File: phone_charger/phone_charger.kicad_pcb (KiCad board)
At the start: 2 copper layers, 22.6 x 30.8 mm, 19 parts, among them J1 Conn_01x02, J2 UE27AC54100, U1 ADP2302

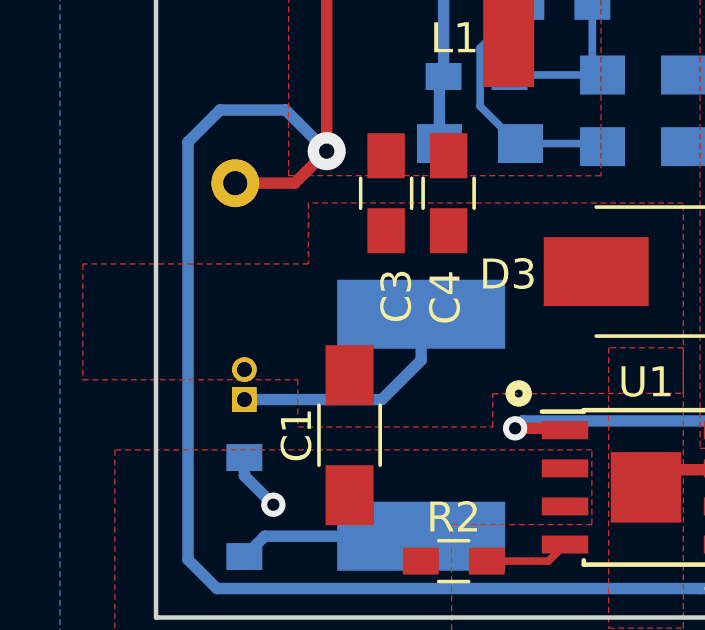
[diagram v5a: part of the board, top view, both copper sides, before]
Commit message: Updated header footprint for charger layout
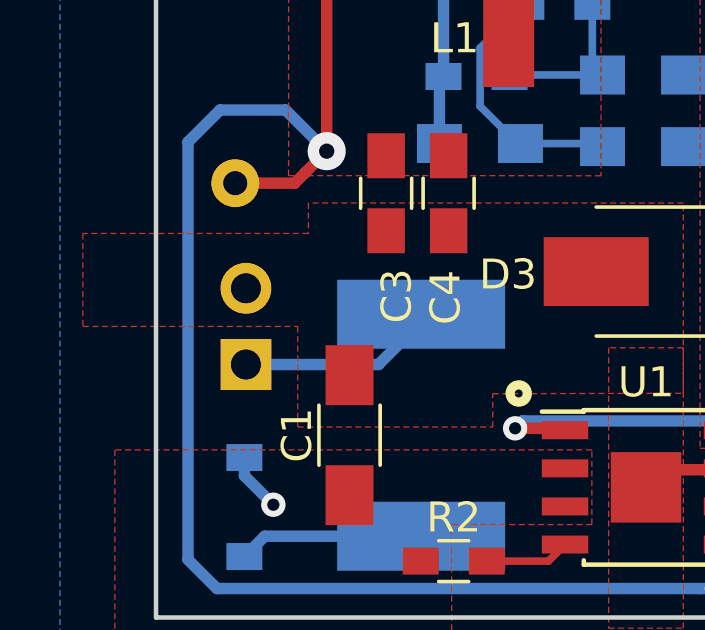
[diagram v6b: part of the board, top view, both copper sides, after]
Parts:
- J1: footprint Pin_Headers:Pin_Header_Straight_1x02_Pitch1.00mm -> Pin_Headers:Pin_Header_Straight_1x02_Pitch2.54mm
- moved J1 1.17 mm to (90.5, 76.0)
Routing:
- net Net-(F1-Pad2): track 7.97 -> 6.69 mm
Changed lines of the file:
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@@
     (add_net VBUS)
+  )
+  (module Pin_Headers:Pin_Header_Straight_1x02_Pitch2.54mm (layer B.Cu)
+    (at 90.5256 75.9968)
+    (descr "Through hole straight pin header, 1x02, 2.54mm pitch, single row")
+    (tags "Through hole pin header THT 1x02 2.54mm single row")
+    (fp_text reference J1 (at 0 2.33) (layer B.SilkS)
+      (effects (font (size 1 1) (thickness 0.15)) (justify mirror))
+    )
+    (fp_text value Conn_01x02 (at 0 -4.87) (layer B.Fab)
+      (effects (font (size 1 1) (thickness 0.15)) (justify mirror))
+    )
+    (fp_text user %R (at 0 -1.27 -90) (layer B.Fab)
+      (effects (font (size 1 1) (thickness 0.15)) (justify mirror))
+    )
+    (fp_line (start 1.8 1.8) (end -1.8 1.8) (layer B.CrtYd) (width 0.05))
+    (fp_line (start 1.8 -4.35) (end 1.8 1.8) (layer B.CrtYd) (width 0.05))
+    (fp_line (start -1.8 -4.35) (end 1.8 -4.35) (layer B.CrtYd) (width 0.05))
+    (fp_line (start -1.8 1.8) (end -1.8 -4.35) (layer B.CrtYd) (width 0.05))
+    (fp_line (start -1.33 1.33) (end 0 1.33) (layer B.SilkS) (width 0.12))
+    (fp_line (start -1.33 0) (end -1.33 1.33) (layer B.SilkS) (width 0.12))
+    (fp_line (start -1.33 -1.27) (end 1.33 -1.27) (layer B.SilkS) (width 0.12))
+    (fp_line (start 1.33 -1.27) (end 1.33 -3.87) (layer B.SilkS) (width 0.12))
+    (fp_line (start -1.33 -1.27) (end -1.33 -3.87) (layer B.SilkS) (width 0.12))
+    (fp_line (start -1.33 -3.87) (end 1.33 -3.87) (layer B.SilkS) (width 0.12))
+    (fp_line (start -1.27 0.635) (end -0.635 1.27) (layer B.Fab) (width 0.1))
+    (fp_line (start -1.27 -3.81) (end -1.27 0.635) (layer B.Fab) (width 0.1))
+    (fp_line (start 1.27 -3.81) (end -1.27 -3.81) (layer B.Fab) (width 0.1))
+    (fp_line (start 1.27 1.27) (end 1.27 -3.81) (layer B.Fab) (width 0.1))
+    (fp_line (start -0.635 1.27) (end 1.27 1.27) (layer B.Fab) (width 0.1))
+    (pad 2 thru_hole oval (at 0 -2.54) (size 1.7 1.7) (drill 1) (layers *.Cu *.Mask)
+      (net 5 EPAD))
+    (pad 1 thru_hole rect (at 0 0) (size 1.7 1.7) (drill 1) (layers *.Cu *.Mask)
+      (net 9 "Net-(F1-Pad2)"))
+    (model ${KISYS3DMOD}/Pin_Headers.3dshapes/Pin_Header_Straight_1x02_Pitch2.54mm.wrl
+      (at (xyz 0 0 0))
+      (scale (xyz 1 1 1))
+      (rotate (xyz 0 0 0))
+    )
   )
   (module Resistor_THT:R_Axial_DIN0207_L6.3mm_D2.5mm_P10.16mm_Horizontal (layer B.Cu)
@@
       (at (xyz 0 0 0))
       (scale (xyz 0.393701 0.393701 0.393701))
-      (rotate (xyz 0 0 0))
-    )
-  )
-  (module Pin_Headers:Pin_Header_Straight_1x02_Pitch1.00mm (layer B.Cu)
-    (at 90.4748 77.1652)
-    (descr "Through hole straight pin header, 1x02, 1.00mm pitch, single row")
-    (tags "Through hole pin header THT 1x02 1.00mm single row")
-    (fp_text reference J1 (at -1.9304 -1.1176 90) (layer B.SilkS)
-      (effects (font (size 1 1) (thickness 0.15)) (justify mirror))
-    )
-    (fp_text value Conn_01x02 (at 0 -2.56) (layer B.Fab)
-      (effects (font (size 1 1) (thickness 0.15)) (justify mirror))
-    )
-    (fp_line (start -0.3175 0.5) (end 0.635 0.5) (layer B.Fab) (width 0.1))
-    (fp_line (start 0.635 0.5) (end 0.635 -1.5) (layer B.Fab) (width 0.1))
-    (fp_line (start 0.635 -1.5) (end -0.635 -1.5) (layer B.Fab) (width 0.1))
-    (fp_line (start -0.635 -1.5) (end -0.635 0.1825) (layer B.Fab) (width 0.1))
-    (fp_line (start -0.635 0.1825) (end -0.3175 0.5) (layer B.Fab) (width 0.1))
-    (fp_line (start -0.695 -1.56) (end -0.394493 -1.56) (layer B.SilkS) (width 0.12))
-    (fp_line (start 0.394493 -1.56) (end 0.695 -1.56) (layer B.SilkS) (width 0.12))
-    (fp_line (start -0.695 -0.685) (end -0.695 -1.56) (layer B.SilkS) (width 0.12))
-    (fp_line (start 0.695 -0.685) (end 0.695 -1.56) (layer B.SilkS) (width 0.12))
-    (fp_line (start -0.695 -0.685) (end -0.608276 -0.685) (layer B.SilkS) (width 0.12))
-    (fp_line (start 0.608276 -0.685) (end 0.695 -0.685) (layer B.SilkS) (width 0.12))
-    (fp_line (start -0.695 0) (end -0.695 0.685) (layer B.SilkS) (width 0.12))
-    (fp_line (start -0.695 0.685) (end 0 0.685) (layer B.SilkS) (width 0.12))
-    (fp_line (start -1.15 1) (end -1.15 -2) (layer B.CrtYd) (width 0.05))
-    (fp_line (start -1.15 -2) (end 1.15 -2) (layer B.CrtYd) (width 0.05))
-    (fp_line (start 1.15 -2) (end 1.15 1) (layer B.CrtYd) (width 0.05))
-    (fp_line (start 1.15 1) (end -1.15 1) (layer B.CrtYd) (width 0.05))
-    (fp_text user %R (at 0 -0.5 -90) (layer B.Fab)
-      (effects (font (size 0.76 0.76) (thickness 0.114)) (justify mirror))
-    )
-    (pad 1 thru_hole rect (at 0 0) (size 0.83 0.83) (drill 0.5) (layers *.Cu *.Mask)
-      (net 9 "Net-(F1-Pad2)"))
-    (pad 2 thru_hole oval (at 0 -1) (size 0.83 0.83) (drill 0.5) (layers *.Cu *.Mask)
-      (net 5 EPAD))
-    (model ${KISYS3DMOD}/Pin_Headers.3dshapes/Pin_Header_Straight_1x02_Pitch1.00mm.wrl
-      (at (xyz 0 0 0))
-      (scale (xyz 1 1 1))
       (rotate (xyz 0 0 0))
     )
@@
   (segment (start 90.4748 79.7052) (end 91.44 80.6704) (width 0.381) (layer B.Cu) (net 8))
   (segment (start 90.4748 79.0976) (end 90.4748 79.7052) (width 0.381) (layer B.Cu) (net 8))
-  (segment (start 96.3676 75.8514) (end 96.3676 74.3204) (width 0.381) (layer B.Cu) (net 9))
-  (segment (start 95.0538 77.1652) (end 96.3676 75.8514) (width 0.381) (layer B.Cu) (net 9))
-  (segment (start 90.4748 77.1652) (end 95.0538 77.1652) (width 0.381) (layer B.Cu) (net 9))
+  (segment (start 94.9452 75.9968) (end 96.3676 74.5744) (width 0.381) (layer B.Cu) (net 9))
+  (segment (start 96.3676 74.5744) (end 96.3676 74.3204) (width 0.381) (layer B.Cu) (net 9))
+  (segment (start 90.5256 75.9968) (end 94.9452 75.9968) (width 0.381) (layer B.Cu) (net 9))
   (segment (start 101.0556 78.0796) (end 101.163001 78.187001) (width 0.254) (layer F.Cu) (net 11))
   (segment (start 108.58 77.6428) (end 108.8136 77.8764) (width 0.381) (layer F.Cu) (net 11))
@@
     (polygon
       (pts
-        (xy 85.09 72.644) (xy 85.09 76.5048) (xy 92.2528 76.5048) (xy 92.2528 78.0796) (xy 98.7552 78.0796)
-        (xy 98.7552 76.969056) (xy 105.1052 76.956087) (xy 105.1052 70.612) (xy 92.6084 70.612) (xy 92.6084 72.644)
+        (xy 85.09 71.628) (xy 85.09 74.7268) (xy 92.2528 74.7268) (xy 92.2528 78.0796) (xy 98.7552 78.0796)
+        (xy 98.7552 76.969056) (xy 105.1052 76.956087) (xy 105.1052 70.612) (xy 92.6084 70.612) (xy 92.6084 71.628)
       )
     )

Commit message: Fix VBUS trace width
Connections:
- net Net-(C2-Pad2) renamed /SWN
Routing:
- net VBUS: track 62.6 -> 54.4 mm
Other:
- net class Power: trace_width 0.381 -> 0.635

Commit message: Fix stuff
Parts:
- moved J2 2.03 mm to (101.1, 56.1)
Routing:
- net VBUS: track 54.4 -> 66.0 mm
- net /D-: track 11.9 -> 14.2 mm
- net /D+: track 8.77 -> 10.9 mm
- net Net-(C2-Pad1): track 12.8 -> 14.8 mm
- net EPAD: track 6.26 -> 6.32 mm, vias 0 -> 6
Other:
- net class Power: via_dia 0.8128 -> 1.27; via_drill 0.4064 -> 0.635
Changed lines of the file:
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@@
   (general
     (thickness 1.5748)
-    (drawings 7)
-    (tracks 61)
+    (drawings 8)
+    (tracks 73)
     (zones 0)
     (modules 19)
@@
     (clearance 0.1524)
     (trace_width 0.635)
-    (via_dia 0.8128)
-    (via_drill 0.4064)
+    (via_dia 1.27)
+    (via_drill 0.635)
     (uvia_dia 0.5588)
     (uvia_drill 0.254)
@@
   )
   (module phone_charger:USB_A_Female_SS-52100-001 (layer B.Cu)
-    (at 101.0072 58.166)
+    (at 101.092 56.134)
     (fp_text reference J2 (at 5.114 -2.9972) (layer B.SilkS)
       (effects (font (size 1 1) (thickness 0.15)) (justify mirror))
@@
       (net 12 /SWN))
   )
+  (gr_poly (pts (xy 102.616 82.931) (xy 105.156 82.931) (xy 105.156 84.328) (xy 102.616 84.328)) (layer F.Mask) (width 0.15))
   (gr_circle (center 109.474 70.0532) (end 109.6264 70.0532) (layer F.SilkS) (width 0.58))
   (gr_circle (center 99.6188 76.962) (end 99.7712 76.962) (layer F.SilkS) (width 0.58))
@@
   (segment (start 96.9772 66.5324) (end 97.114 66.3956) (width 0.381) (layer B.Cu) (net 1))
   (segment (start 96.9772 68.6308) (end 96.9772 66.5324) (width 0.381) (layer B.Cu) (net 1))
-  (segment (start 97.114 61.2692) (end 97.5072 60.876) (width 0.381) (layer B.Cu) (net 1))
-  (segment (start 97.114 66.3956) (end 97.114 61.2692) (width 0.381) (layer B.Cu) (net 1))
   (via (at 106.222802 83.4644) (size 0.8128) (drill 0.4064) (layers F.Cu B.Cu) (net 1))
   (segment (start 106.563001 81.997001) (end 106.563001 83.124201) (width 0.381) (layer F.Cu) (net 1))
@@
   (segment (start 92.1512 69.9516) (end 92.5068 69.596) (width 0.381) (layer F.Cu) (net 1))
   (segment (start 90.17 69.9516) (end 92.1512 69.9516) (width 0.381) (layer F.Cu) (net 1))
-  (segment (start 97.5072 60.876) (end 97.5072 64.5956) (width 2.286) (layer F.Cu) (net 1))
+  (segment (start 97.592 65.9176) (end 97.114 66.3956) (width 0.635) (layer B.Cu) (net 1))
+  (segment (start 97.592 58.844) (end 97.592 65.9176) (width 0.635) (layer B.Cu) (net 1))
+  (segment (start 97.592 58.844) (end 95.207 58.844) (width 1.27) (layer F.Cu) (net 1))
+  (segment (start 93.218 60.833) (end 93.218 68.8848) (width 1.27) (layer F.Cu) (net 1))
+  (segment (start 95.207 58.844) (end 93.218 60.833) (width 1.27) (layer F.Cu) (net 1))
   (segment (start 88.9 58.5216) (end 90.17 59.7916) (width 0.254) (layer F.Cu) (net 2))
   (segment (start 88.9 56.134) (end 88.9 58.5216) (width 0.254) (layer F.Cu) (net 2))
   (segment (start 100.0072 63.9244) (end 99.8728 64.0588) (width 0.254) (layer B.Cu) (net 3))
-  (segment (start 100.0072 60.891) (end 100.0072 63.9244) (width 0.254) (layer B.Cu) (net 3))
   (segment (start 98.332999 67.386599) (end 99.5772 68.6308) (width 0.254) (layer B.Cu) (net 3))
   (segment (start 99.5772 68.6308) (end 99.6772 68.6308) (width 0.254) (layer B.Cu) (net 3))
@@
   (segment (start 102.3112 68.6308) (end 102.4128 68.7324) (width 0.254) (layer B.Cu) (net 3))
   (segment (start 99.6772 68.6308) (end 102.3112 68.6308) (width 0.254) (layer B.Cu) (net 3))
+  (segment (start 99.8728 59.0782) (end 100.092 58.859) (width 0.254) (layer B.Cu) (net 3))
+  (segment (start 99.8728 64.0588) (end 99.8728 59.0782) (width 0.254) (layer B.Cu) (net 3))
   (segment (start 103.275501 79.504501) (end 104.450501 79.504501) (width 0.381) (layer F.Cu) (net 4))
   (segment (start 104.450501 79.504501) (end 104.450501 80.679501) (width 0.381) (layer F.Cu) (net 4))
   (segment (start 104.450501 80.679501) (end 103.275501 80.679501) (width 0.381) (layer F.Cu) (net 4))
   (segment (start 106.515501 79.504501) (end 106.563001 79.457001) (width 0.381) (layer F.Cu) (net 4))
-  (segment (start 104.450501 79.504501) (end 106.515501 79.504501) (width 0.381) (layer F.Cu) (net 4))
   (segment (start 102.802 72.898) (end 102.202 72.898) (width 0.381) (layer F.Cu) (net 4))
+  (segment (start 104.498001 79.457001) (end 104.450501 79.504501) (width 0.635) (layer F.Cu) (net 4))
+  (segment (start 106.563001 79.457001) (end 104.498001 79.457001) (width 0.635) (layer F.Cu) (net 4))
+  (via (at 93.345 71.882) (size 1.27) (drill 0.635) (layers F.Cu B.Cu) (net 4))
+  (via (at 99.187 71.882) (size 1.27) (drill 0.635) (layers F.Cu B.Cu) (net 4))
+  (via (at 96.647 76.835) (size 1.27) (drill 0.635) (layers F.Cu B.Cu) (net 4))
+  (via (at 101.219 75.565) (size 1.27) (drill 0.635) (layers F.Cu B.Cu) (net 4))
+  (via (at 103.759 75.565) (size 1.27) (drill 0.635) (layers F.Cu B.Cu) (net 4))
+  (via (at 103.759 77.978) (size 1.27) (drill 0.635) (layers F.Cu B.Cu) (net 4))
   (segment (start 102.0072 63.9932) (end 102.0728 64.0588) (width 0.254) (layer B.Cu) (net 5))
-  (segment (start 102.0072 60.866) (end 102.0072 63.9932) (width 0.254) (layer B.Cu) (net 5))
   (segment (start 102.0728 66.0048) (end 102.4128 66.3448) (width 0.254) (layer B.Cu) (net 5))
   (segment (start 102.0728 64.0588) (end 102.0728 66.0048) (width 0.254) (layer B.Cu) (net 5))
   (segment (start 99.3648 66.3448) (end 99.314 66.3956) (width 0.254) (layer B.Cu) (net 5))
   (segment (start 102.4128 66.3448) (end 99.3648 66.3448) (width 0.254) (layer B.Cu) (net 5))
+  (segment (start 102.092 64.0396) (end 102.0728 64.0588) (width 0.254) (layer B.Cu) (net 5))
+  (segment (start 102.092 58.834) (end 102.092 64.0396) (width 0.254) (layer B.Cu) (net 5))
   (segment (start 100.610002 82.55) (end 101.163001 81.997001) (width 0.254) (layer F.Cu) (net 6))
   (segment (start 98.552 82.55) (end 100.610002 82.55) (width 0.254) (layer F.Cu) (net 6))
-  (via (at 91.44 80.6704) (size 0.8128) (drill 0.4064) (layers F.Cu B.Cu) (net 7))
-  (segment (start 90.4748 79.7052) (end 91.44 80.6704) (width 0.381) (layer B.Cu) (net 7))
-  (segment (start 90.4748 79.0976) (end 90.4748 79.7052) (width 0.381) (layer B.Cu) (net 7))
-  (segment (start 94.9452 75.9968) (end 96.3676 74.5744) (width 0.381) (layer B.Cu) (net 8))
-  (segment (start 96.3676 74.5744) (end 96.3676 74.3204) (width 0.381) (layer B.Cu) (net 8))
-  (segment (start 90.5256 75.9968) (end 94.9452 75.9968) (width 0.381) (layer B.Cu) (net 8))
+  (segment (start 90.5276 79.0976) (end 91.694 80.264) (width 1.27) (layer B.Cu) (net 7))
+  (via (at 91.694 80.264) (size 2.032) (drill 1.016) (layers F.Cu B.Cu) (net 7))
+  (segment (start 90.4748 79.0976) (end 90.5276 79.0976) (width 1.27) (layer B.Cu) (net 7))
+  (segment (start 94.6912 75.9968) (end 96.3676 74.3204) (width 1.27) (layer B.Cu) (net 8))
+  (segment (start 90.5256 75.9968) (end 94.6912 75.9968) (width 1.27) (layer B.Cu) (net 8))
   (segment (start 101.0556 78.0796) (end 101.163001 78.187001) (width 0.254) (layer F.Cu) (net 10))
-  (segment (start 108.58 77.6428) (end 108.8136 77.8764) (width 0.381) (layer F.Cu) (net 10))
-  (via (at 108.8136 77.8764) (size 0.8128) (drill 0.4064) (layers F.Cu B.Cu) (net 10))
-  (segment (start 108.58 76.4032) (end 108.58 77.6428) (width 0.381) (layer F.Cu) (net 10))
-  (via (at 99.498648 78.123551) (size 0.8128) (drill 0.4064) (layers F.Cu B.Cu) (net 10))
-  (segment (start 99.745799 77.8764) (end 99.498648 78.123551) (width 0.381) (layer B.Cu) (net 10))
-  (segment (start 108.8136 77.8764) (end 99.745799 77.8764) (width 0.381) (layer B.Cu) (net 10))
-  (segment (start 101.099551 78.123551) (end 101.163001 78.187001) (width 0.381) (layer F.Cu) (net 10))
-  (segment (start 99.498648 78.123551) (end 101.099551 78.123551) (width 0.381) (layer F.Cu) (net 10))
-  (segment (start 91.152 81.7204) (end 90.4748 82.3976) (width 0.381) (layer B.Cu) (net 11))
-  (segment (start 96.3676 81.7204) (end 91.152 81.7204) (width 0.381) (layer B.Cu) (net 11))
+  (segment (start 108.58 77.719) (end 108.966 78.105) (width 0.635) (layer F.Cu) (net 10))
+  (segment (start 108.58 76.4032) (end 108.58 77.719) (width 0.635) (layer F.Cu) (net 10))
+  (via (at 108.966 78.105) (size 1.27) (drill 0.635) (layers F.Cu B.Cu) (net 10))
+  (segment (start 101.163001 78.187001) (end 99.753001 78.187001) (width 0.635) (layer F.Cu) (net 10))
+  (segment (start 99.314 77.748) (end 99.314 77.597) (width 0.635) (layer F.Cu) (net 10))
+  (segment (start 99.753001 78.187001) (end 99.314 77.748) (width 0.635) (layer F.Cu) (net 10))
+  (via (at 99.314 77.597) (size 1.27) (drill 0.635) (layers F.Cu B.Cu) (net 10))
+  (segment (start 100.203 76.708) (end 99.314 77.597) (width 0.635) (layer B.Cu) (net 10))
+  (segment (start 107.569 76.708) (end 100.203 76.708) (width 0.635) (layer B.Cu) (net 10))
+  (segment (start 108.966 78.105) (end 107.569 76.708) (width 0.635) (layer B.Cu) (net 10))
+  (segment (start 95.6904 82.3976) (end 90.4748 82.3976) (width 1.27) (layer B.Cu) (net 11))
+  (segment (start 96.3676 81.7204) (end 95.6904 82.3976) (width 1.27) (layer B.Cu) (net 11))
   (zone (net 12) (net_name /SWN) (layer F.Cu) (hatch edge 0.508)
     (connect_pads yes (clearance 0.508))
